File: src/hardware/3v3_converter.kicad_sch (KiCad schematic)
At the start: 3 parts, among them U26 TPS7A2033DQNR

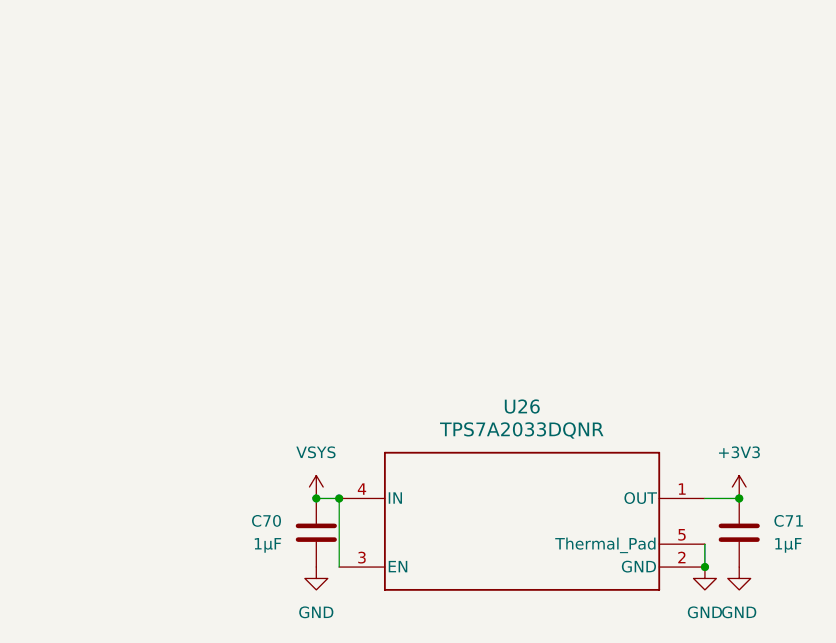
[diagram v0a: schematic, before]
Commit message: Replaced global labels with pin headers
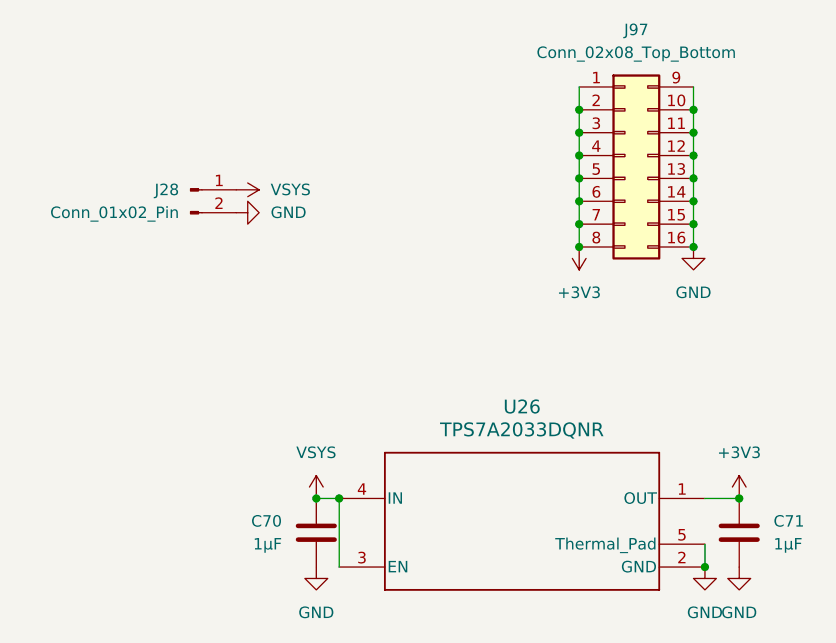
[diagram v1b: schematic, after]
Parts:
- added J28: Conn_01x02_Pin, symbol Connector:Conn_01x02_Pin
- added J97: Conn_02x08_Top_Bottom, symbol Connector_Generic:Conn_02x08_Top_Bottom
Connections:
- net +3V3: now also J97.1 (Pin_1), J97.2 (Pin_2), J97.3 (Pin_3), J97.4 (Pin_4), J97.5 (Pin_5), J97.6 (Pin_6), J97.7 (Pin_7), J97.8 (Pin_8)
- net GND: now also J28.2 (Pin_2), J97.10 (Pin_10), J97.11 (Pin_11), J97.12 (Pin_12), J97.13 (Pin_13), J97.14 (Pin_14), J97.15 (Pin_15), J97.16 (Pin_16), J97.9 (Pin_9)
- net VSYS: now also J28.1 (Pin_1)

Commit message: Reannotated schematic
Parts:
- renumbered C70 to C65, C71 to C66, J28 to J74, J97 to J75, U26 to U27
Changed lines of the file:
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@@
 		(dnp no)
 		(fields_autoplaced yes)
-		(property "Reference" "J28"
+		(property "Reference" "J74"
 			(at 111.76 67.3099 0)
 			(effects
@@
 			(project "raywatch"
 				(path "/7b654ee8-2a53-4d39-8b7d-32c7bb3cb0ed/1d8b2961-678d-411b-851f-e266eaec5e93"
-					(reference "J28")
+					(reference "J74")
 					(unit 1)
 				)
@@
 		(dnp no)
 		(fields_autoplaced yes)
-		(property "Reference" "U26"
+		(property "Reference" "U27"
 			(at 149.86 91.44 0)
 			(effects
@@
 			(project "raywatch"
 				(path "/7b654ee8-2a53-4d39-8b7d-32c7bb3cb0ed/1d8b2961-678d-411b-851f-e266eaec5e93"
-					(reference "U26")
+					(reference "U27")
 					(unit 1)
 				)
@@
 		(dnp no)
 		(fields_autoplaced yes)
-		(property "Reference" "#PWR0352"
+		(property "Reference" "#PWR0387"
 			(at 173.99 115.57 0)
 			(effects
@@
 			(project "raywatch"
 				(path "/7b654ee8-2a53-4d39-8b7d-32c7bb3cb0ed/1d8b2961-678d-411b-851f-e266eaec5e93"
-					(reference "#PWR0352")
+					(reference "#PWR0387")
 					(unit 1)
 				)
@@
 		(dnp no)
 		(fields_autoplaced yes)
-		(property "Reference" "#PWR0460"
+		(property "Reference" "#PWR0380"
 			(at 124.46 69.85 0)
 			(effects
@@
 			(project "raywatch"
 				(path "/7b654ee8-2a53-4d39-8b7d-32c7bb3cb0ed/1d8b2961-678d-411b-851f-e266eaec5e93"
-					(reference "#PWR0460")
+					(reference "#PWR0380")
 					(unit 1)
 				)
@@
 		(dnp no)
 		(fields_autoplaced yes)
-		(property "Reference" "#PWR0459"
+		(property "Reference" "#PWR0379"
 			(at 114.3 67.31 0)
 			(effects
@@
 			(project "raywatch"
 				(path "/7b654ee8-2a53-4d39-8b7d-32c7bb3cb0ed/1d8b2961-678d-411b-851f-e266eaec5e93"
-					(reference "#PWR0459")
+					(reference "#PWR0379")
 					(unit 1)
 				)
@@
 		(dnp no)
 		(fields_autoplaced yes)
-		(property "Reference" "C70"
+		(property "Reference" "C65"
 			(at 123.19 104.1399 0)
 			(effects
@@
 			(project "raywatch"
 				(path "/7b654ee8-2a53-4d39-8b7d-32c7bb3cb0ed/1d8b2961-678d-411b-851f-e266eaec5e93"
-					(reference "C70")
+					(reference "C65")
 					(unit 1)
 				)
@@
 		(dnp no)
 		(fields_autoplaced yes)
-		(property "Reference" "#PWR068"
+		(property "Reference" "#PWR0384"
 			(at 168.91 80.01 0)
 			(effects
@@
 			(project "raywatch"
 				(path "/7b654ee8-2a53-4d39-8b7d-32c7bb3cb0ed/1d8b2961-678d-411b-851f-e266eaec5e93"
-					(reference "#PWR068")
+					(reference "#PWR0384")
 					(unit 1)
 				)
@@
 		(dnp no)
 		(fields_autoplaced yes)
-		(property "Reference" "#PWR0348"
+		(property "Reference" "#PWR0381"
 			(at 127 105.41 0)
 			(effects
@@
 			(project "raywatch"
 				(path "/7b654ee8-2a53-4d39-8b7d-32c7bb3cb0ed/1d8b2961-678d-411b-851f-e266eaec5e93"
-					(reference "#PWR0348")
+					(reference "#PWR0381")
 					(unit 1)
 				)
@@
 		(dnp no)
 		(fields_autoplaced yes)
-		(property "Reference" "J97"
+		(property "Reference" "J75"
 			(at 162.56 49.53 0)
 			(effects
@@
 			(project "raywatch"
 				(path "/7b654ee8-2a53-4d39-8b7d-32c7bb3cb0ed/1d8b2961-678d-411b-851f-e266eaec5e93"
-					(reference "J97")
+					(reference "J75")
 					(unit 1)
 				)
@@
 		(dnp no)
 		(fields_autoplaced yes)
-		(property "Reference" "#PWR0350"
+		(property "Reference" "#PWR0385"
 			(at 170.18 115.57 0)
 			(effects
@@
 			(project "raywatch"
 				(path "/7b654ee8-2a53-4d39-8b7d-32c7bb3cb0ed/1d8b2961-678d-411b-851f-e266eaec5e93"
-					(reference "#PWR0350")
+					(reference "#PWR0385")
 					(unit 1)
 				)
@@
 		(dnp no)
 		(fields_autoplaced yes)
-		(property "Reference" "#PWR0351"
+		(property "Reference" "#PWR0386"
 			(at 173.99 105.41 0)
 			(effects
@@
 			(project "raywatch"
 				(path "/7b654ee8-2a53-4d39-8b7d-32c7bb3cb0ed/1d8b2961-678d-411b-851f-e266eaec5e93"
-					(reference "#PWR0351")
+					(reference "#PWR0386")
 					(unit 1)
 				)
@@
 		(dnp no)
 		(fields_autoplaced yes)
-		(property "Reference" "#PWR067"
+		(property "Reference" "#PWR0383"
 			(at 156.21 69.85 0)
 			(effects
@@
 			(project "raywatch"
 				(path "/7b654ee8-2a53-4d39-8b7d-32c7bb3cb0ed/1d8b2961-678d-411b-851f-e266eaec5e93"
-					(reference "#PWR067")
+					(reference "#PWR0383")
 					(unit 1)
 				)
@@
 		(dnp no)
 		(fields_autoplaced yes)
-		(property "Reference" "#PWR0349"
+		(property "Reference" "#PWR0382"
 			(at 127 115.57 0)
 			(effects
@@
 			(project "raywatch"
 				(path "/7b654ee8-2a53-4d39-8b7d-32c7bb3cb0ed/1d8b2961-678d-411b-851f-e266eaec5e93"
-					(reference "#PWR0349")
+					(reference "#PWR0382")
 					(unit 1)
 				)
@@
 		(dnp no)
 		(fields_autoplaced yes)
-		(property "Reference" "C71"
+		(property "Reference" "C66"
 			(at 177.8 104.1399 0)
 			(effects
@@
 			(project "raywatch"
 				(path "/7b654ee8-2a53-4d39-8b7d-32c7bb3cb0ed/1d8b2961-678d-411b-851f-e266eaec5e93"
-					(reference "C71")
-					(unit 1)
-				)
+					(reference "C66")
+					(unit 1)
+				)

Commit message: Assigned pin header footprints
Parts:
- J74: footprint (none) -> Connector_PinHeader_2.54mm:PinHeader_1x02_P2.54mm_Horizontal
- J75: footprint (none) -> Connector_PinHeader_2.54mm:PinHeader_1x16_P2.54mm_Vertical
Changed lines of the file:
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@@
 			)
 		)
-		(property "Footprint" ""
+		(property "Footprint" "Connector_PinHeader_2.54mm:PinHeader_1x02_P2.54mm_Horizontal"
 			(at 113.03 67.31 0)
 			(effects
@@
 			)
 		)
-		(property "Footprint" ""
+		(property "Footprint" "Connector_PinHeader_2.54mm:PinHeader_1x16_P2.54mm_Vertical"
 			(at 161.29 63.5 0)
 			(effects

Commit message: Fixed footprints
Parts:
- J75: footprint Connector_PinHeader_2.54mm:PinHeader_1x16_P2.54mm_Vertical -> Connector_PinHeader_2.54mm:PinHeader_2x08_P2.54mm_Vertical
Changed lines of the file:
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@@
 			)
 		)
-		(property "Footprint" "Connector_PinHeader_2.54mm:PinHeader_1x16_P2.54mm_Vertical"
+		(property "Footprint" "Connector_PinHeader_2.54mm:PinHeader_2x08_P2.54mm_Vertical"
 			(at 161.29 63.5 0)
 			(effects

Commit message: Changed pin headers to vertical
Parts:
- J74: footprint Connector_PinHeader_2.54mm:PinHeader_1x02_P2.54mm_Horizontal -> Connector_PinHeader_2.54mm:PinHeader_1x04_P2.54mm_Vertical
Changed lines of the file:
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@@
 			)
 		)
-		(property "Footprint" "Connector_PinHeader_2.54mm:PinHeader_1x02_P2.54mm_Horizontal"
+		(property "Footprint" "Connector_PinHeader_2.54mm:PinHeader_1x04_P2.54mm_Vertical"
 			(at 113.03 67.31 0)
 			(effects

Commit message: Fixed connector footprints; Changed conectors from 2.54 to 1.27
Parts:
- J72: renamed from J74; footprint Connector_PinHeader_2.54mm:PinHeader_1x04_P2.54mm_Vertical -> Connector_PinHeader_1.27mm:PinHeader_1x02_P1.27mm_Vertical
- J73: renamed from J75; footprint Connector_PinHeader_2.54mm:PinHeader_2x08_P2.54mm_Vertical -> Connector_PinHeader_1.27mm:PinHeader_2x08_P1.27mm_Vertical
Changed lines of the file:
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@@
 		(dnp no)
 		(fields_autoplaced yes)
-		(property "Reference" "J74"
+		(property "Reference" "J72"
 			(at 111.76 67.3099 0)
 			(effects
@@
 			)
 		)
-		(property "Footprint" "Connector_PinHeader_2.54mm:PinHeader_1x04_P2.54mm_Vertical"
+		(property "Footprint" "Connector_PinHeader_1.27mm:PinHeader_1x02_P1.27mm_Vertical"
 			(at 113.03 67.31 0)
 			(effects
@@
 			(project "raywatch"
 				(path "/7b654ee8-2a53-4d39-8b7d-32c7bb3cb0ed/1d8b2961-678d-411b-851f-e266eaec5e93"
-					(reference "J74")
+					(reference "J72")
 					(unit 1)
 				)
@@
 		(dnp no)
 		(fields_autoplaced yes)
-		(property "Reference" "#PWR0389"
+		(property "Reference" "#PWR0391"
 			(at 173.99 115.57 0)
 			(effects
@@
 			(project "raywatch"
 				(path "/7b654ee8-2a53-4d39-8b7d-32c7bb3cb0ed/1d8b2961-678d-411b-851f-e266eaec5e93"
-					(reference "#PWR0389")
+					(reference "#PWR0391")
 					(unit 1)
 				)
@@
 		(dnp no)
 		(fields_autoplaced yes)
-		(property "Reference" "#PWR0382"
+		(property "Reference" "#PWR0384"
 			(at 124.46 69.85 0)
 			(effects
@@
 			(project "raywatch"
 				(path "/7b654ee8-2a53-4d39-8b7d-32c7bb3cb0ed/1d8b2961-678d-411b-851f-e266eaec5e93"
-					(reference "#PWR0382")
+					(reference "#PWR0384")
 					(unit 1)
 				)
@@
 		(dnp no)
 		(fields_autoplaced yes)
-		(property "Reference" "#PWR0381"
+		(property "Reference" "#PWR0383"
 			(at 114.3 67.31 0)
 			(effects
@@
 			(project "raywatch"
 				(path "/7b654ee8-2a53-4d39-8b7d-32c7bb3cb0ed/1d8b2961-678d-411b-851f-e266eaec5e93"
-					(reference "#PWR0381")
+					(reference "#PWR0383")
 					(unit 1)
 				)
@@
 		(dnp no)
 		(fields_autoplaced yes)
-		(property "Reference" "#PWR0386"
+		(property "Reference" "#PWR0388"
 			(at 168.91 80.01 0)
 			(effects
@@
 			(project "raywatch"
 				(path "/7b654ee8-2a53-4d39-8b7d-32c7bb3cb0ed/1d8b2961-678d-411b-851f-e266eaec5e93"
-					(reference "#PWR0386")
+					(reference "#PWR0388")
 					(unit 1)
 				)
@@
 		(dnp no)
 		(fields_autoplaced yes)
-		(property "Reference" "#PWR0383"
+		(property "Reference" "#PWR0385"
 			(at 127 105.41 0)
 			(effects
@@
 			(project "raywatch"
 				(path "/7b654ee8-2a53-4d39-8b7d-32c7bb3cb0ed/1d8b2961-678d-411b-851f-e266eaec5e93"
-					(reference "#PWR0383")
+					(reference "#PWR0385")
 					(unit 1)
 				)
@@
 		(dnp no)
 		(fields_autoplaced yes)
-		(property "Reference" "J75"
+		(property "Reference" "J73"
 			(at 162.56 49.53 0)
 			(effects
@@
 			)
 		)
-		(property "Footprint" "Connector_PinHeader_2.54mm:PinHeader_2x08_P2.54mm_Vertical"
+		(property "Footprint" "Connector_PinHeader_1.27mm:PinHeader_2x08_P1.27mm_Vertical"
 			(at 161.29 63.5 0)
 			(effects
@@
 			(project "raywatch"
 				(path "/7b654ee8-2a53-4d39-8b7d-32c7bb3cb0ed/1d8b2961-678d-411b-851f-e266eaec5e93"
-					(reference "J75")
+					(reference "J73")
 					(unit 1)
 				)
@@
 		(dnp no)
 		(fields_autoplaced yes)
-		(property "Reference" "#PWR0387"
+		(property "Reference" "#PWR0389"
 			(at 170.18 115.57 0)
 			(effects
@@
 			(project "raywatch"
 				(path "/7b654ee8-2a53-4d39-8b7d-32c7bb3cb0ed/1d8b2961-678d-411b-851f-e266eaec5e93"
-					(reference "#PWR0387")
+					(reference "#PWR0389")
 					(unit 1)
 				)
@@
 		(dnp no)
 		(fields_autoplaced yes)
-		(property "Reference" "#PWR0388"
+		(property "Reference" "#PWR0390"
 			(at 173.99 105.41 0)
 			(effects
@@
 			(project "raywatch"
 				(path "/7b654ee8-2a53-4d39-8b7d-32c7bb3cb0ed/1d8b2961-678d-411b-851f-e266eaec5e93"
-					(reference "#PWR0388")
+					(reference "#PWR0390")
 					(unit 1)
 				)
@@
 		(dnp no)
 		(fields_autoplaced yes)
-		(property "Reference" "#PWR0385"
+		(property "Reference" "#PWR0387"
 			(at 156.21 69.85 0)
 			(effects
@@
 			(project "raywatch"
 				(path "/7b654ee8-2a53-4d39-8b7d-32c7bb3cb0ed/1d8b2961-678d-411b-851f-e266eaec5e93"
-					(reference "#PWR0385")
+					(reference "#PWR0387")
 					(unit 1)
 				)
@@
 		(dnp no)
 		(fields_autoplaced yes)
-		(property "Reference" "#PWR0384"
+		(property "Reference" "#PWR0386"
 			(at 127 115.57 0)
 			(effects
@@
 			(project "raywatch"
 				(path "/7b654ee8-2a53-4d39-8b7d-32c7bb3cb0ed/1d8b2961-678d-411b-851f-e266eaec5e93"
-					(reference "#PWR0384")
-					(unit 1)
-				)
+					(reference "#PWR0386")
+					(unit 1)
+				)

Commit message: Fixes; Added TPM PCB
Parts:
- C65, C66: footprint Capacitor_SMD:C_0504_1310Metric -> Capacitor_SMD:C_0402_1005Metric
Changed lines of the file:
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@@
 			)
 		)
-		(property "Footprint" "Capacitor_SMD:C_0504_1310Metric"
+		(property "Footprint" "Capacitor_SMD:C_0402_1005Metric"
 			(at 126.0348 109.22 0)
 			(effects
@@
 			)
 		)
-		(property "Footprint" "Capacitor_SMD:C_0504_1310Metric"
+		(property "Footprint" "Capacitor_SMD:C_0402_1005Metric"
 			(at 174.9552 109.22 0)
 			(effects
